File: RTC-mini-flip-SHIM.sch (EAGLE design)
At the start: 12 parts, among them IC1 DS3231/SO, IC2 DS3231M

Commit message: Use more locking pin headers. Moved some traces.
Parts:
- J1, J2: device SparkFun-Connectors:CONN_05LOCK -> _my_locked_connectors:CONN_05LOCK
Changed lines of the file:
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@@
 <layer number="115" name="ReferenceISLANDS" color="7" fill="1" visible="no" active="yes"/>
 <layer number="116" name="Patch_BOT" color="9" fill="4" visible="no" active="yes"/>
+<layer number="117" name="PM_Ref" color="7" fill="1" visible="no" active="no"/>
 <layer number="118" name="Rect_Pads" color="7" fill="1" visible="no" active="no"/>
+<layer number="119" name="PF_Ref" color="7" fill="1" visible="no" active="no"/>
+<layer number="120" name="WFL_Ref" color="7" fill="1" visible="no" active="no"/>
 <layer number="121" name="_tsilk" color="7" fill="1" visible="no" active="yes"/>
 <layer number="122" name="_bsilk" color="7" fill="1" visible="no" active="yes"/>
@@
 <layer number="128" name="_bValues" color="7" fill="1" visible="no" active="yes"/>
 <layer number="129" name="Mask" color="7" fill="1" visible="yes" active="yes"/>
+<layer number="130" name="SMDSTROOK" color="7" fill="1" visible="no" active="no"/>
 <layer number="131" name="tAdjust" color="7" fill="1" visible="no" active="yes"/>
 <layer number="132" name="bAdjust" color="7" fill="1" visible="no" active="yes"/>
+<layer number="133" name="bottom_silk" color="7" fill="1" visible="no" active="no"/>
+<layer number="134" name="silk_top" color="7" fill="1" visible="no" active="no"/>
+<layer number="135" name="silk_bottom" color="7" fill="1" visible="no" active="no"/>
+<layer number="136" name="silktop" color="7" fill="1" visible="no" active="no"/>
+<layer number="137" name="silkbottom" color="7" fill="1" visible="no" active="no"/>
+<layer number="138" name="EEE" color="7" fill="1" visible="no" active="no"/>
+<layer number="139" name="_tKeepout" color="7" fill="1" visible="no" active="no"/>
+<layer number="140" name="mbKeepout" color="7" fill="1" visible="no" active="no"/>
+<layer number="141" name="ASSEMBLY_TOP" color="7" fill="1" visible="no" active="no"/>
+<layer number="142" name="mbRestrict" color="7" fill="1" visible="no" active="no"/>
+<layer number="143" name="PLACE_BOUND_TOP" color="7" fill="1" visible="no" active="no"/>
 <layer number="144" name="Drill_legend" color="7" fill="1" visible="no" active="yes"/>
+<layer number="145" name="DrillLegend_01-16" color="7" fill="1" visible="no" active="no"/>
+<layer number="146" name="DrillLegend_01-20" color="7" fill="1" visible="no" active="no"/>
+<layer number="147" name="PIN_NUMBER" color="7" fill="1" visible="no" active="no"/>
+<layer number="148" name="DrillLegend_01-20" color="7" fill="1" visible="no" active="no"/>
+<layer number="149" name="DrillLegend_02-15" color="7" fill="1" visible="no" active="no"/>
 <layer number="150" name="Notes" color="7" fill="1" visible="no" active="yes"/>
 <layer number="151" name="HeatSink" color="7" fill="1" visible="no" active="yes"/>
@@
 <layer number="164" name="tRubout" color="7" fill="1" visible="yes" active="yes"/>
 <layer number="165" name="bRubout" color="7" fill="1" visible="yes" active="yes"/>
+<layer number="166" name="AntennaArea" color="7" fill="1" visible="no" active="no"/>
 <layer number="167" name="Fiducials" color="7" fill="1" visible="yes" active="yes"/>
+<layer number="168" name="4mmHeightArea" color="7" fill="1" visible="no" active="no"/>
 <layer number="169" name="internal" color="7" fill="1" visible="yes" active="yes"/>
+<layer number="191" name="mNets" color="7" fill="1" visible="no" active="no"/>
+<layer number="192" name="mBusses" color="7" fill="1" visible="no" active="no"/>
+<layer number="193" name="mPins" color="7" fill="1" visible="no" active="no"/>
+<layer number="194" name="mSymbols" color="7" fill="1" visible="no" active="no"/>
+<layer number="195" name="mNames" color="7" fill="1" visible="no" active="no"/>
+<layer number="196" name="mValues" color="7" fill="1" visible="no" active="no"/>
 <layer number="199" name="Contour" color="7" fill="1" visible="no" active="yes"/>
 <layer number="200" name="200bmp" color="1" fill="10" visible="no" active="yes"/>
@@
 <part name="SUPPLY4" library="SparkFun-PowerSymbols" library_urn="urn:adsk.eagle:library:530" deviceset="3.3V" device=""/>
 <part name="SUPPLY5" library="SparkFun-PowerSymbols" library_urn="urn:adsk.eagle:library:530" deviceset="3.3V" device=""/>
-<part name="J1" library="SparkFun-Connectors" library_urn="urn:adsk.eagle:library:513" deviceset="CONN_05" device="LOCK" package3d_urn="urn:adsk.eagle:package:38105/1"/>
-<part name="J2" library="SparkFun-Connectors" library_urn="urn:adsk.eagle:library:513" deviceset="CONN_05" device="LOCK" package3d_urn="urn:adsk.eagle:package:38105/1"/>
+<part name="J1" library="_my_locked_connectors" deviceset="CONN_05" device="LOCK"/>
+<part name="J2" library="_my_locked_connectors" deviceset="CONN_05" device="LOCK"/>
 <part name="SUPPLY6" library="SparkFun-PowerSymbols" library_urn="urn:adsk.eagle:library:530" deviceset="3.3V" device=""/>
 <part name="GND5" library="SparkFun-PowerSymbols" library_urn="urn:adsk.eagle:library:530" deviceset="GND" device=""/>

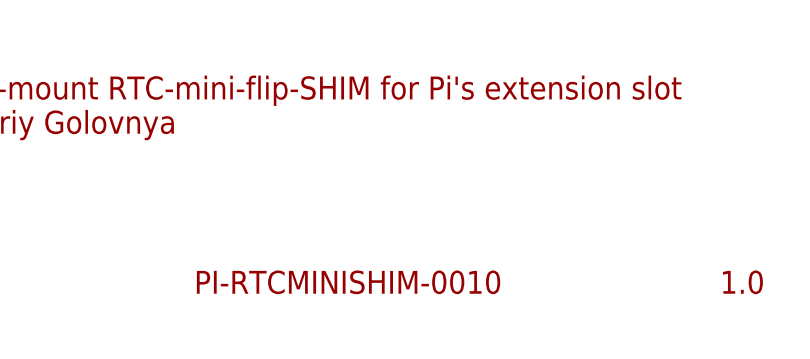
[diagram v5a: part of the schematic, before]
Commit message: Simplified document names. Generated PDF schematics.
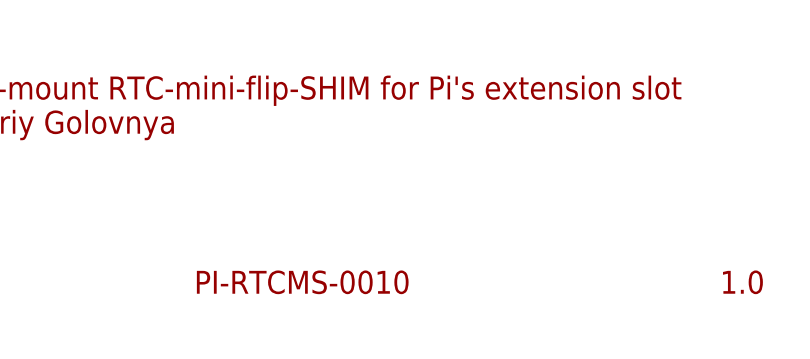
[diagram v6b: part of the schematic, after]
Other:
- note added: "PI-RTCMS-0010"
- note removed: "PI-RTCMINISHIM-0010"
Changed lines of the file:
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@@
 <plain>
 <text x="256.54" y="7.62" size="2.54" layer="94">1.0</text>
-<text x="198.12" y="7.62" size="2.54" layer="94">PI-RTCMINISHIM-0010</text>
+<text x="198.12" y="7.62" size="2.54" layer="94">PI-RTCMS-0010</text>
 <text x="165.1" y="25.4" size="2.54" layer="94">Double-mount RTC-mini-flip-SHIM for Pi's extension slot
 (c) Andriy Golovnya</text>
